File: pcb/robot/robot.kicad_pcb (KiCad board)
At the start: 4 copper layers, 80 x 70 mm, 318 parts, among them IC1 TPS22998RYZR, J1 USBC_Receptacle_SMD_RA, J2 Conn_01x05, J3 Conn_01x06_MountingPin, J4 USB4151-GF-C, J5 Conn_01x06_MountingPin, J8 Conn_01x02, J9 Conn_01x16, Q1 Q_NMOS_GDS, Q2 EFC8811R-TF, Q3 AS2312, Q4 YJL3416A, Q5 SN74AHC125RGYR, Q6 SN74AHC125RGYR, Q7 Q_NMOS_GDS, SW1 SW_SPST, U1 STWLC38JRM, U12 BQ27742YZFR-G1, U13 MAX77976EFD+, U14 MAX77642ANA+, U18 AP33771DKZ-13, U2 W25Q128JVS, U25 TVS0500DRV, U26 TPD1E05U06, U27 TPD1E05U06, U28 TPD1E05U06, U29 TPD1E05U06, U3 RP2040, U4 NCP3901, U5 LSF0102DCTR, U6 MAX77857BEWB+, U7 AP2502KTR-G1, U8 DRV8830DRCR, U9 DRV8830DRCR, Y1 ECS-120-8-36-CKM-TR3

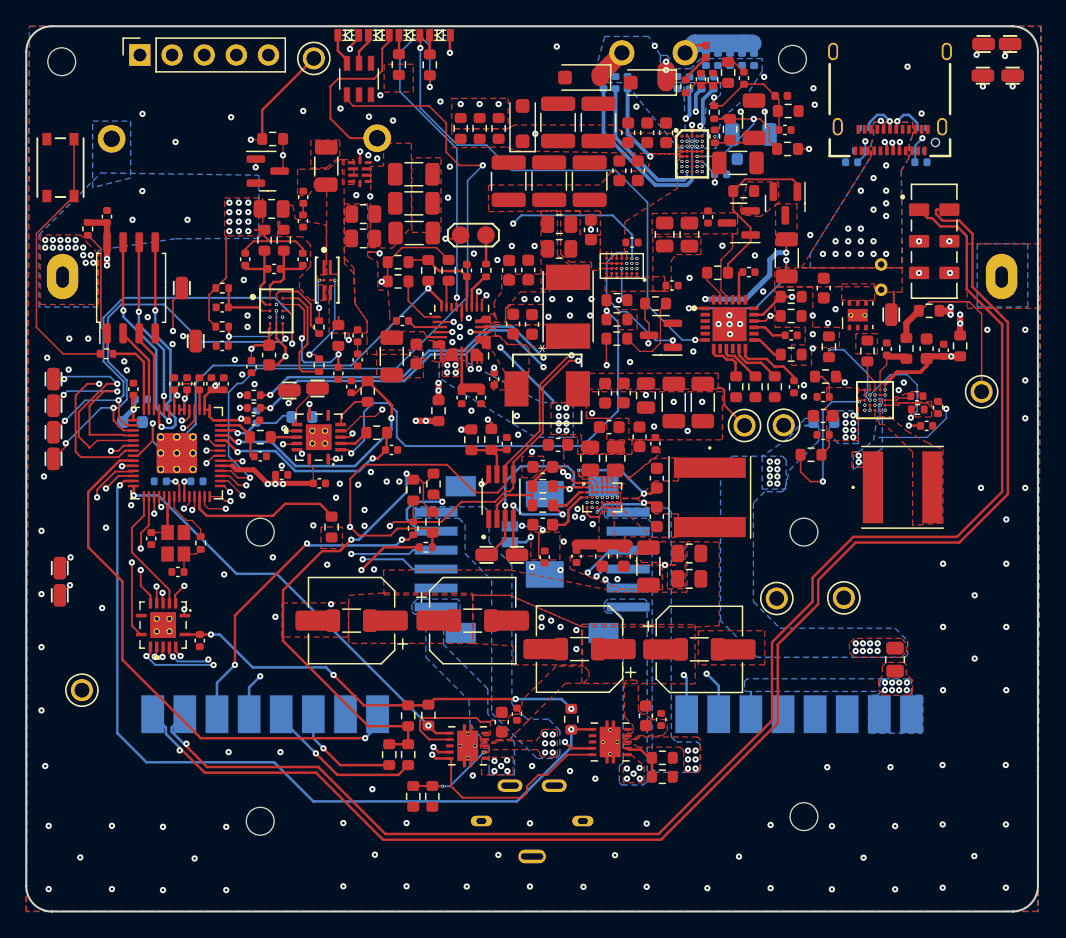
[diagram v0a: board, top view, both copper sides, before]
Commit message: Modification and replacement of MAX77642ANA
The MAX77642ANA was replaced with the LDO XC6206 and the TPS63021DSJR. Rerouting and Gerber updates were performed.
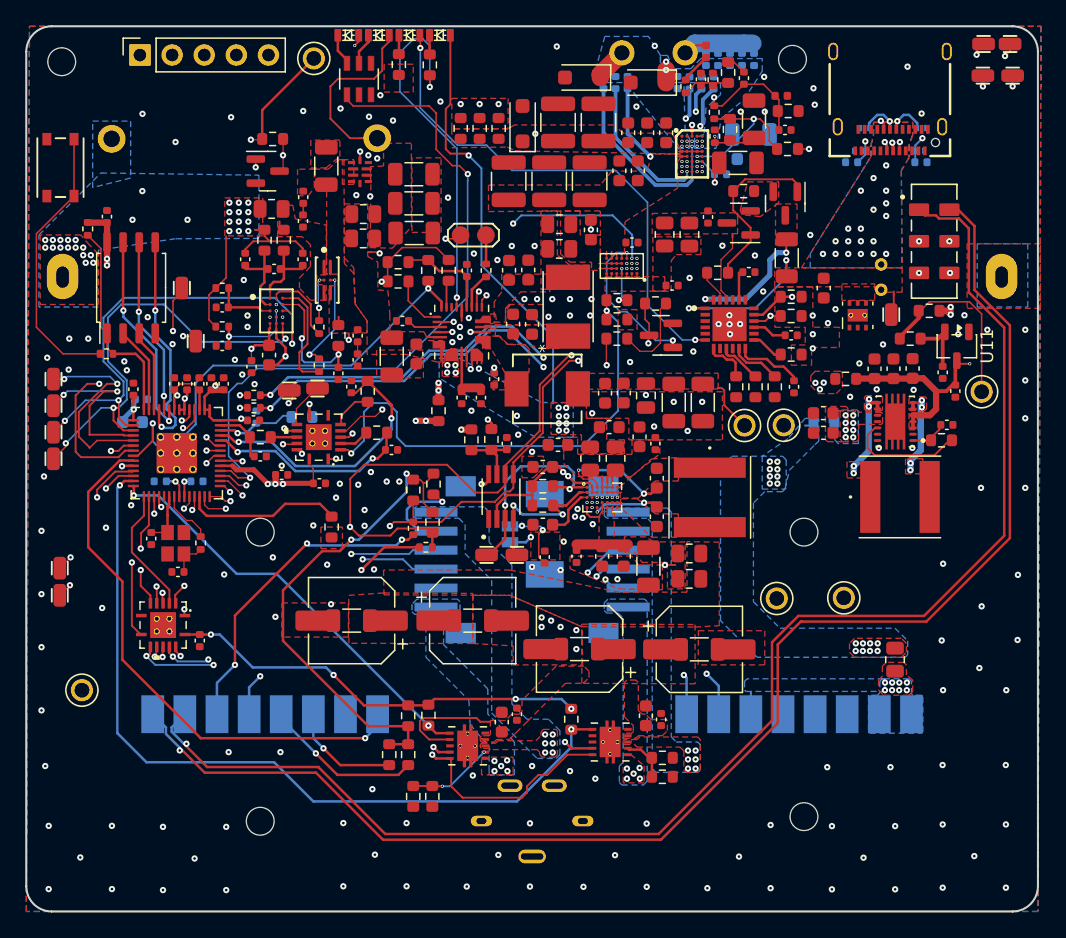
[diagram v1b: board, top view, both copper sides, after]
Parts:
- removed C84: 10nF, robot:C_0402_1005Metric
- removed C85: 0.1uF, robot:C_0402_1005Metric
- removed C87: 22uF, robot:C_0603_1608Metric
- removed R53: 113K, robot:R_0603_1608Metric
- removed R55: 14k, robot:R_0603_1608Metric
- removed R9: 80.6k, robot:R_0402_1005Metric
- removed R93: 0, robot:R_0603_1608Metric
- removed U14: MAX77642ANA+, robot:Maxim-N252B2-1-0-A-MFG
- added C45: 10uF, robot:C_0603_1608Metric, F.Cu at (123.0, 122.2)
- added C46: 1uF, robot:C_0402_1005Metric, F.Cu at (133.5, 118.8)
- added U10: TPS63021DSJR, robot:IC_TPS63021DSJR, F.Cu at (128.7, 121.3)
- added U11: XC6206PxxxMR, Package_TO_SOT_SMD:SOT-23-3, F.Cu at (133.6, 115.3)
- C4: value 1uF -> 10uF; footprint robot:C_0402_1005Metric -> robot:C_0603_1608Metric
- C94, C95: value 1uF -> 22uF; footprint robot:C_0402_1005Metric -> robot:C_0603_1608Metric
- moved R92 10.5 mm to (132.4, 122.7), turned to 0 degrees
- moved R94 9.42 mm to (124.8, 117.9), turned to 180 degrees
- moved C95 6.11 mm to (127.1, 117.1), turned to 90 degrees
- moved C92 5.91 mm to (132.8, 121.5), turned to 0 degrees
- moved C88 4.79 mm to (132.5, 117.4), turned to -90 degrees
- moved C93 3.06 mm to (128.6, 117.1)
- moved C94 2.22 mm to (130.1, 117.1), turned to 90 degrees
- moved C4 1.28 mm to (123.0, 120.6), turned to 0 degrees
- moved R91 0.83 mm to (129.9, 114.7), turned to 180 degrees
- moved L3 0.79 mm to (129.1, 127.2)
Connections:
- C4 pad 1: /LDOs/SYS -> GND
- C4 pad 2: GND -> /LDOs/SYS
- C92 pad 1: Net-(D2-A) -> Net-(U10-VINA)
- C94 pad 1: Net-(U14-SBB0) -> Net-(D2-A)
- C95 pad 1: Net-(U14-SBB2) -> Net-(D2-A)
- R92 pad 1: Net-(U14-EN1) -> Net-(U10-VINA)
- R92 pad 2: /LDOs/SYS -> Net-(U10-EN)
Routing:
- net /3V3: track 161.0 -> 147.3 mm, vias 10 -> 11
- net Net-(U14-ENLDO): track 12.7 -> 0.00 mm, vias 2 -> 0
- net Net-(U10-EN): track 0.00 -> 9.23 mm
- net Net-(U14-RSET_LDO): track 8.21 -> 0.00 mm, vias 2 -> 0
- net /LDOs/SYS: track 7.13 -> 0.38 mm
- net Net-(U14-RSET_IPK): track 6.67 -> 0.00 mm, vias 2 -> 0
- net Net-(U10-L2_6): track 0.73 -> 7.17 mm, vias 0 -> 4
- net Net-(D2-A): track 91.1 -> 96.1 mm, vias 4 -> 2
- net Net-(U14-BST): track 4.59 -> 0.00 mm
- net Net-(U14-SBB2): track 4.53 -> 0.00 mm, vias 2 -> 0
- net Net-(U14-EN1): track 3.98 -> 0.00 mm, vias 2 -> 0
- net Net-(U10-VINA): track 0.00 -> 3.01 mm
- net Net-(U14-RSET_SBB1): track 2.84 -> 0.00 mm
- net Net-(U14-SBB0): track 2.16 -> 0.00 mm
- net /LED_EN: track 57.6 -> 55.8 mm
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- added copper zone on F.Cu, net /3V3
- added copper zone on In2.Cu, net /3V3
- added copper zone on F.Cu, net Net-(D2-A)
- removed copper zone on B.Cu, net Net-(U10-L1_8)
